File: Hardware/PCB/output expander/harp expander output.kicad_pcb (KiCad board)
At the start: 2 copper layers, 124.5 x 80.4 mm, 167 parts, among them IC1 ATXMEGA128A1U-AU, IC10 SN74LVC1G125DBVT, IC2 USBLC6-2SC6, IC3 FT232RL-REEL, IC4 TLV70033DDCR, IC5 TLV70033DDCR, IC6 SI8621BC-B-ISR, IC7 SN74LVC1G125DBVT, IC8 SN74LVC1G125DBVT, IC9 SN74LVC1G125DBVT, T10 BC850C,215, T11 BC850C,215, T12 BC850C,215, T13 BC850C,215, T2 BC850C,215, T3 BC850C,215, T4 BC850C,215, T5 BC850C,215, T6 BC850C,215, T7 BC850C,215, T8 BC850C,215, T9 BC850C,215, U1 SN74LVC4245APWR, U2 SN74LVC4245APWR, U3 74HCT125D,653

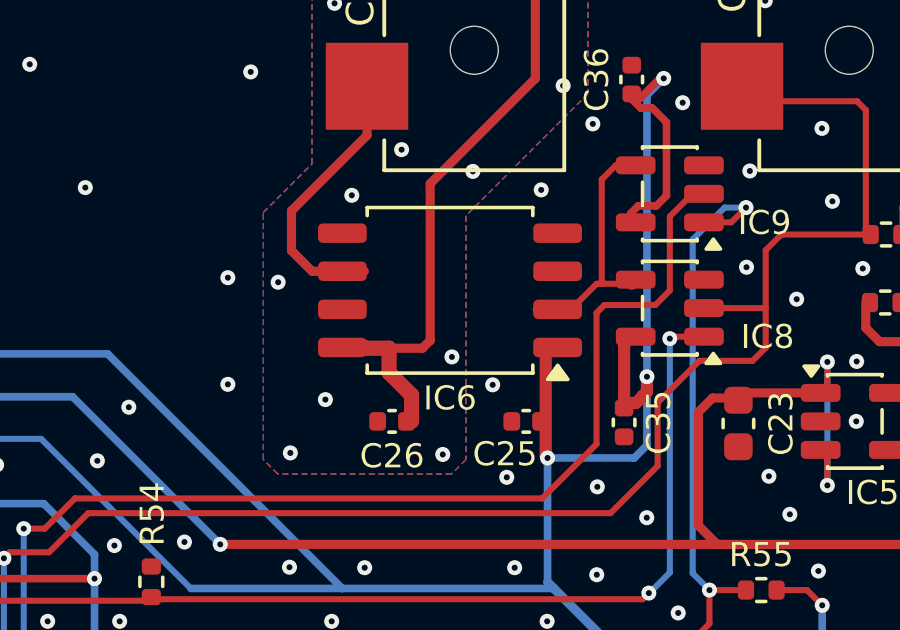
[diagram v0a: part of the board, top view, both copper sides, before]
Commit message: Fixed IC6 MPN and footprint, and U1-2 MPN
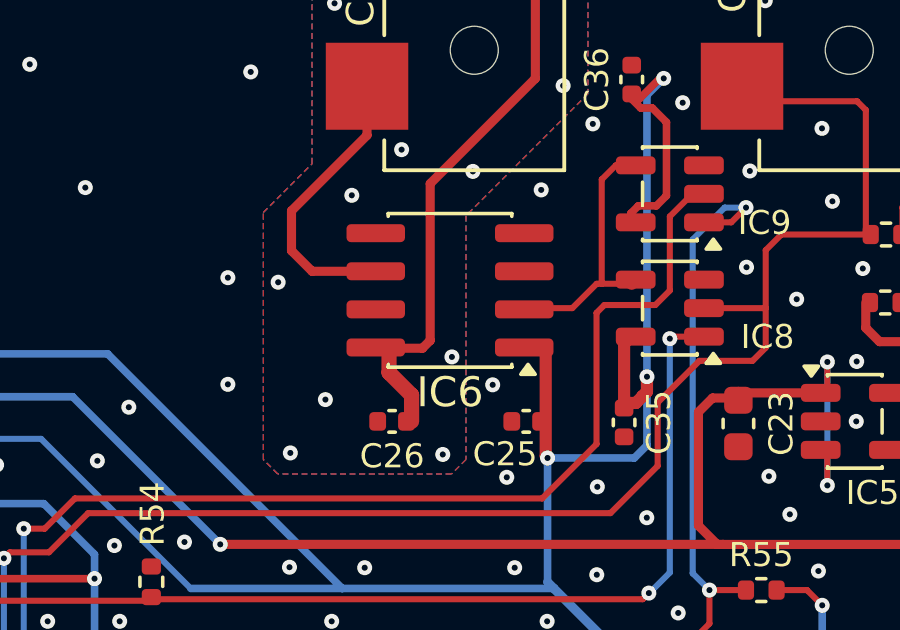
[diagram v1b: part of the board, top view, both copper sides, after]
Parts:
- IC6: value SI8621BC-B-ISR -> SI8610BC-B-IS; footprint Package_SO:SOIC-8_5.3x5.3mm_P1.27mm -> Package_SO:SOIC-8_3.9x4.9mm_P1.27mm
- U1, U2: value SN74LVC4245APWR -> SN74LVC8T245DWR
